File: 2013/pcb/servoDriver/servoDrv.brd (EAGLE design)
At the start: 20.3 x 16.5 mm, 9 parts, among them X1 22-23-2041

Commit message: servodriveriin tehty muutoksia. Sense-vastukset paremmin gnd-planeen.
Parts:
- moved RSENS_B 10.0 mm to (8.39, 11.5), turned to 0 degrees
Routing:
- net N$4: track 8.46 -> 0.00 mm
- net VCC: track 0.00 -> 7.28 mm
- removed copper zone on layer 16, net VCC
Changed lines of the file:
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@@
 <plain>
 <wire x1="0" y1="0" x2="20.32" y2="0" width="0" layer="20"/>
-<wire x1="20.32" y1="0" x2="20.32" y2="16.5" width="0" layer="20"/>
 <wire x1="20.32" y1="16.5" x2="0" y2="16.5" width="0" layer="20"/>
 <wire x1="0" y1="16.5" x2="0" y2="0" width="0" layer="20"/>
@@
 </element>
 <element name="RSENS_A" library="resistor" package="R1206" value="" x="8.45" y="4.06" rot="MR180"/>
-<element name="RSENS_B" library="resistor" package="R1206" value="" x="12.94" y="2.61" rot="MR90"/>
+<element name="RSENS_B" library="resistor" package="R1206" value="" x="8.39" y="11.54" rot="MR0"/>
 <element name="RIN_A" library="resistor" package="R0805" value="" x="7.96" y="3.63"/>
 <element name="RIN_B" library="resistor" package="R0805" value="" x="8.01" y="11.23"/>
@@
 <contactref element="C2" pad="1"/>
 <contactref element="X1" pad="2"/>
-<polygon width="0.3048" layer="16">
-<vertex x="-0.2" y="10"/>
-<vertex x="-0.2" y="16.8"/>
-<vertex x="20.6" y="16.8"/>
-<vertex x="20.6" y="10.8"/>
-<vertex x="8.2" y="10.8"/>
-<vertex x="8.2" y="8.2"/>
-<vertex x="-0.2" y="8.2"/>
-</polygon>
-<wire x1="7.27" y1="8.51" x2="9.3884" y2="8.455" width="0" layer="19" extent="16-16"/>
+<wire x1="2.34015625" y1="8.87005" x2="4.63995" y2="8.87005" width="1.016" layer="16"/>
+<wire x1="4.63995" y1="8.87005" x2="5.07" y2="8.44" width="1.016" layer="16"/>
+<wire x1="5.07" y1="8.44" x2="7.2" y2="8.44" width="1.016" layer="16"/>
+<wire x1="7.2" y1="8.44" x2="7.27" y2="8.51" width="1.016" layer="16"/>
+<wire x1="7.27" y1="8.51" x2="9.3334" y2="8.51" width="1.016" layer="16"/>
+<wire x1="9.3334" y1="8.51" x2="9.3884" y2="8.455" width="1.016" layer="16"/>
 </signal>
 <signal name="GND">
@@
 <contactref element="C2" pad="2"/>
 <contactref element="X1" pad="3"/>
-<polygon width="0.3048" layer="16">
-<vertex x="-0.2" y="16.6"/>
-<vertex x="20.6" y="16.6"/>
-<vertex x="20.6" y="11.4"/>
-<vertex x="13.4" y="11.4"/>
-<vertex x="13.4" y="4.2"/>
-<vertex x="20.6" y="4.2"/>
-<vertex x="20.6" y="-0.4"/>
-<vertex x="-0.4" y="-0.4"/>
-<vertex x="-0.4" y="16.6"/>
-</polygon>
 <polygon width="0.3048" layer="1">
 <vertex x="-0.2" y="16.6"/>
@@
 <vertex x="-0.2" y="-0.2"/>
 </polygon>
+<polygon width="0.3048" layer="16">
+<vertex x="-0.2" y="16.4"/>
+<vertex x="20.4" y="16.4"/>
+<vertex x="20.4" y="16.2"/>
+<vertex x="20.4" y="0"/>
+<vertex x="0" y="0"/>
+<vertex x="0" y="0.2"/>
+<vertex x="-0.2" y="0.2"/>
+</polygon>
 </signal>
 <signal name="N$1">
@@
 <contactref element="U1" pad="4"/>
 <contactref element="RSENS_B" pad="2"/>
-<wire x1="9.3884" y1="9.725" x2="11.6" y2="9.725" width="0.3048" layer="16"/>
-<wire x1="11.6" y1="9.725" x2="11.6" y2="5.372" width="0.3048" layer="16"/>
-<wire x1="11.6" y1="5.372" x2="12.94" y2="4.032" width="0.3048" layer="16"/>
+<wire x1="6.968" y1="11.54" x2="9.3884" y2="9.725" width="0" layer="19" extent="16-16"/>
 </signal>
 <signal name="N$6">

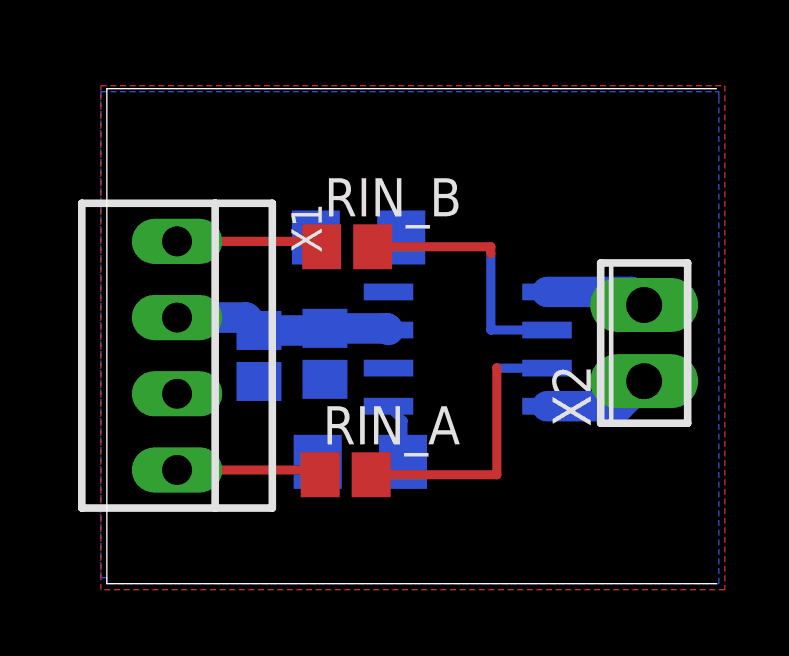
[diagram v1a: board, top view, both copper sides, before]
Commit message: servodriverin skemaa muutettu, lisätty tvs:t inputteihin ja poistettu sense-vastukset. Myös puuttuvat viat lisätty.
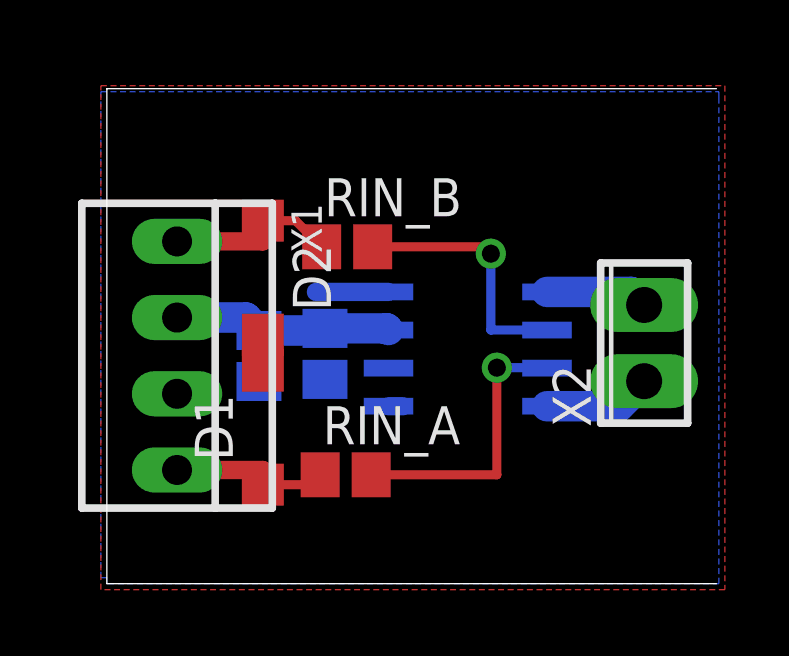
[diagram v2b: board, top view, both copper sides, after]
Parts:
- removed RSENS_A, RSENS_B: (no value), resistor:R1206
- added D1, D2: (no value), diode:SOD123
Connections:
- removed net N$3: RSENS_A.2, U1.1
- removed net N$4: RSENS_B.2, U1.4
- net GND: now also D1.A, D2.A, U1.1, U1.4; no longer RSENS_A.1, RSENS_B.1
- net N$5: now also D1.C
- net N$8: now also D2.C
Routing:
- net GND: track 0.00 -> 2.90 mm
- net N$3: track 2.06 -> 0.00 mm
- net N$8: track 4.89 -> 5.87 mm
- net N$7: track 8.59 -> 8.45 mm, vias 0 -> 1
- net N$6: vias 0 -> 1
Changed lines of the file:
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@@
 <attribute name="OC_FARNELL" value="unknown" x="31.88" y="24.53" size="1.778" layer="27" rot="R90" display="off"/>
 </element>
-<element name="RSENS_A" library="resistor" package="R1206" value="" x="8.45" y="4.06" rot="MR180"/>
-<element name="RSENS_B" library="resistor" package="R1206" value="" x="8.39" y="11.54" rot="MR0"/>
 <element name="RIN_A" library="resistor" package="R0805" value="" x="7.96" y="3.63"/>
 <element name="RIN_B" library="resistor" package="R0805" value="" x="8.01" y="11.23"/>
 <element name="C1" library="resistor" package="C0805" value="" x="5.07" y="7.59" rot="MR270"/>
 <element name="C2" library="resistor" package="C0805" value="" x="7.27" y="7.66" rot="MR270"/>
+<element name="D1" library="diode" package="SOD123" value="" x="5.2" y="5.2" rot="R90"/>
+<element name="D2" library="diode" package="SOD123" value="" x="5.2" y="10.2" rot="R270"/>
 </elements>
 <signals>
@@
 </signal>
 <signal name="GND">
-<contactref element="U1" pad="2"/>
-<contactref element="RSENS_B" pad="1"/>
-<contactref element="RSENS_A" pad="1"/>
 <contactref element="C1" pad="2"/>
 <contactref element="C2" pad="2"/>
@@
 <vertex x="-0.2" y="0.2"/>
 </polygon>
+<contactref element="U1" pad="1"/>
+<wire x1="9.3884" y1="5.915" x2="9.872" y2="5.915" width="0.6096" layer="16"/>
+<contactref element="U1" pad="4"/>
+<wire x1="9.3884" y1="9.725" x2="6.968" y2="9.725" width="0.6096" layer="16"/>
+<contactref element="U1" pad="2"/>
+<contactref element="D1" pad="A"/>
+<contactref element="D2" pad="A"/>
 </signal>
 <signal name="N$1">
@@
 <wire x1="17.475" y1="9.725" x2="17.91" y2="9.29" width="1.016" layer="16"/>
 </signal>
-<signal name="N$3">
-<contactref element="RSENS_A" pad="2"/>
-<contactref element="U1" pad="1"/>
-<wire x1="9.3884" y1="5.915" x2="9.872" y2="5.4314" width="0.3048" layer="16"/>
-<wire x1="9.872" y1="5.4314" x2="9.872" y2="4.06" width="0.3048" layer="16"/>
-</signal>
-<signal name="N$4">
-<contactref element="U1" pad="4"/>
-<contactref element="RSENS_B" pad="2"/>
-<wire x1="6.968" y1="11.54" x2="9.3884" y2="9.725" width="0" layer="19" extent="16-16"/>
-</signal>
 <signal name="N$6">
 <contactref element="RIN_A" pad="2"/>
 <contactref element="U1" pad="7"/>
-<wire x1="8.81" y1="3.63" x2="13" y2="3.63" width="0.3048" layer="1"/>
-<wire x1="13" y1="3.63" x2="13" y2="7.2" width="0.3048" layer="1"/>
-<wire x1="14.6716" y1="7.185" x2="13" y2="7.185" width="0.3048" layer="16"/>
-<wire x1="13" y1="7.185" x2="13" y2="7.2" width="0.3048" layer="16"/>
-<wire x1="13" y1="7.2" x2="13" y2="7.2" width="0" layer="19" extent="1-16"/>
+<wire x1="14.6716" y1="7.185" x2="14.6716" y2="7.2" width="0.3048" layer="16"/>
+<wire x1="14.6716" y1="7.2" x2="13" y2="7.2" width="0.3048" layer="16"/>
+<via x="13" y="7.2" extent="1-16" drill="0.6" shape="square"/>
+<wire x1="13" y1="7.2" x2="13" y2="3.63" width="0.3048" layer="1"/>
+<wire x1="13" y1="3.63" x2="8.81" y2="3.63" width="0.3048" layer="1"/>
 </signal>
 <signal name="N$7">
 <contactref element="RIN_B" pad="2"/>
 <contactref element="U1" pad="6"/>
-<wire x1="8.86" y1="11.23" x2="12.8" y2="11.23" width="0.3048" layer="1"/>
-<wire x1="12.8" y1="11.23" x2="12.8" y2="11" width="0.3048" layer="1"/>
-<wire x1="14.6716" y1="8.455" x2="12.8" y2="8.455" width="0.3048" layer="16"/>
-<wire x1="12.8" y1="8.455" x2="12.8" y2="11" width="0.3048" layer="16"/>
-<wire x1="12.8" y1="11" x2="12.8" y2="11" width="0" layer="19" extent="1-16"/>
+<wire x1="8.86" y1="11.23" x2="12.57" y2="11.23" width="0.3048" layer="1"/>
+<wire x1="12.57" y1="11.23" x2="12.8" y2="11" width="0.3048" layer="1"/>
+<via x="12.8" y="11" extent="1-16" drill="0.6" shape="square"/>
+<wire x1="12.8" y1="11" x2="12.8" y2="8.455" width="0.3048" layer="16"/>
+<wire x1="12.8" y1="8.455" x2="14.6716" y2="8.455" width="0.3048" layer="16"/>
 </signal>
 <signal name="N$8">
 <contactref element="X1" pad="1"/>
 <contactref element="RIN_B" pad="1"/>
-<wire x1="6.97995" y1="11.41005" x2="7.16" y2="11.23" width="1.016" layer="1"/>
-<wire x1="2.34015625" y1="11.41005" x2="6.97995" y2="11.41005" width="0.3048" layer="1"/>
+<contactref element="D2" pad="C"/>
+<wire x1="2.34015625" y1="11.41005" x2="5.2" y2="11.41005" width="0.6096" layer="1"/>
+<wire x1="5.2" y1="11.41005" x2="5.2" y2="12.1" width="0.6096" layer="1"/>
+<wire x1="7.16" y1="11.23" x2="6.29" y2="12.1" width="0.3048" layer="1"/>
+<wire x1="6.29" y1="12.1" x2="5.2" y2="12.1" width="0.3048" layer="1"/>
 </signal>
 <signal name="N$5">
 <contactref element="X1" pad="4"/>
 <contactref element="RIN_A" pad="1"/>
-<wire x1="2.34015625" y1="3.79005" x2="7.11" y2="3.79005" width="0.3048" layer="1"/>
-<wire x1="7.11" y1="3.79005" x2="7.11" y2="3.63" width="0.3048" layer="1"/>
+<contactref element="D1" pad="C"/>
+<wire x1="2.34015625" y1="3.79005" x2="5.2" y2="3.79005" width="0.6096" layer="1"/>
+<wire x1="5.2" y1="3.79005" x2="5.2" y2="3.3" width="0.6096" layer="1"/>
+<wire x1="7.11" y1="3.63" x2="6.78" y2="3.3" width="0.3048" layer="1"/>
+<wire x1="6.78" y1="3.3" x2="5.2" y2="3.3" width="0.3048" layer="1"/>
 </signal>
 </signals>

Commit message: Lisää muutoksia servodriveriin, board outline lisätty.
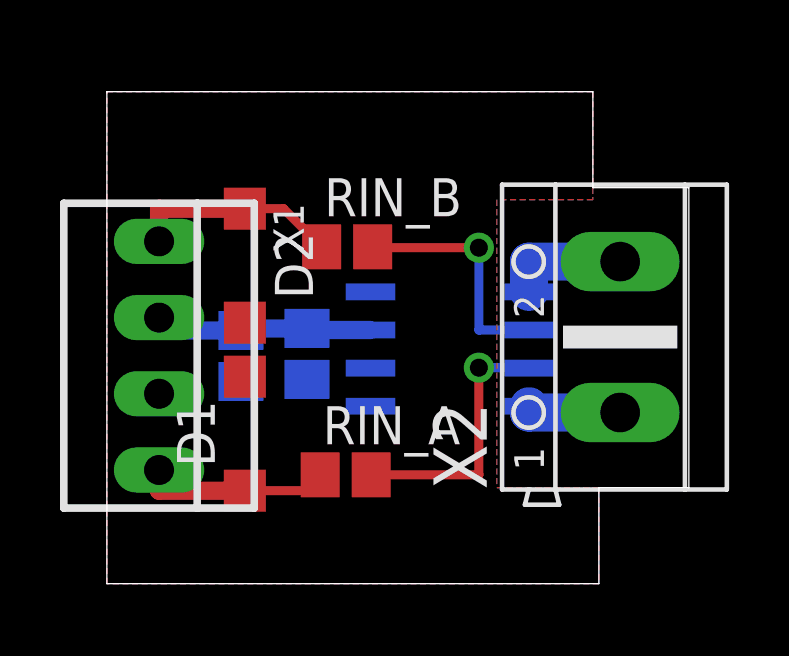
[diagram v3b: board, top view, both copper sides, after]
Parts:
- X2: device con-phoenix-254:2POL254 -> con-ptr500:AK500/2
- moved X2 0.82 mm to (17.1, 8.22)
- moved D2 0.72 mm to (4.60, 10.6)
- moved D1 0.63 mm to (4.60, 5.00)
- moved C1 0.60 mm to (4.47, 7.59)
- moved X1 0.60 mm to (1.74, 7.60)
- moved C2 0.60 mm to (6.67, 7.66)
- moved U1 0.60 mm to (11.4, 7.82)
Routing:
- net GND: track 2.90 -> 0.00 mm
- net N$8: track 5.87 -> 7.04 mm
- net N$5: track 5.40 -> 6.28 mm
- net N$2: track 3.42 -> 4.05 mm
- net N$6: track 9.45 -> 10.0 mm
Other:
- board size 20.3 x 16.5 mm -> 19.4 x 16.4 mm

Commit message: viimeisin versio servodriverista
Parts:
- C1: value (none) -> 100n
- C2: value (none) -> 1u
- D1, D2: value (none) -> PTVS6V0S1UR
- RIN_A, RIN_B: value (none) -> 100
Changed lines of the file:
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@@
 <attribute name="OC_FARNELL" value="unknown" x="31.08" y="24.73" size="1.778" layer="27" rot="R90" display="off"/>
 </element>
-<element name="RIN_A" library="resistor" package="R0805" value="" x="7.96" y="3.63"/>
-<element name="RIN_B" library="resistor" package="R0805" value="" x="8.01" y="11.23"/>
-<element name="C1" library="resistor" package="C0805" value="" x="4.47" y="7.59" rot="MR270"/>
-<element name="C2" library="resistor" package="C0805" value="" x="6.67" y="7.66" rot="MR270"/>
-<element name="D1" library="diode" package="SOD123" value="" x="4.6" y="5" rot="R90"/>
-<element name="D2" library="diode" package="SOD123" value="" x="4.6" y="10.6" rot="R270"/>
+<element name="RIN_A" library="resistor" package="R0805" value="100" x="7.96" y="3.63"/>
+<element name="RIN_B" library="resistor" package="R0805" value="100" x="8.01" y="11.23"/>
+<element name="C1" library="resistor" package="C0805" value="100n" x="4.47" y="7.59" rot="MR270"/>
+<element name="C2" library="resistor" package="C0805" value="1u" x="6.67" y="7.66" rot="MR270"/>
+<element name="D1" library="diode" package="SOD123" value="PTVS6V0S1UR" x="4.6" y="5" rot="R90"/>
+<element name="D2" library="diode" package="SOD123" value="PTVS6V0S1UR" x="4.6" y="10.6" rot="R270"/>
 </elements>
 <signals>

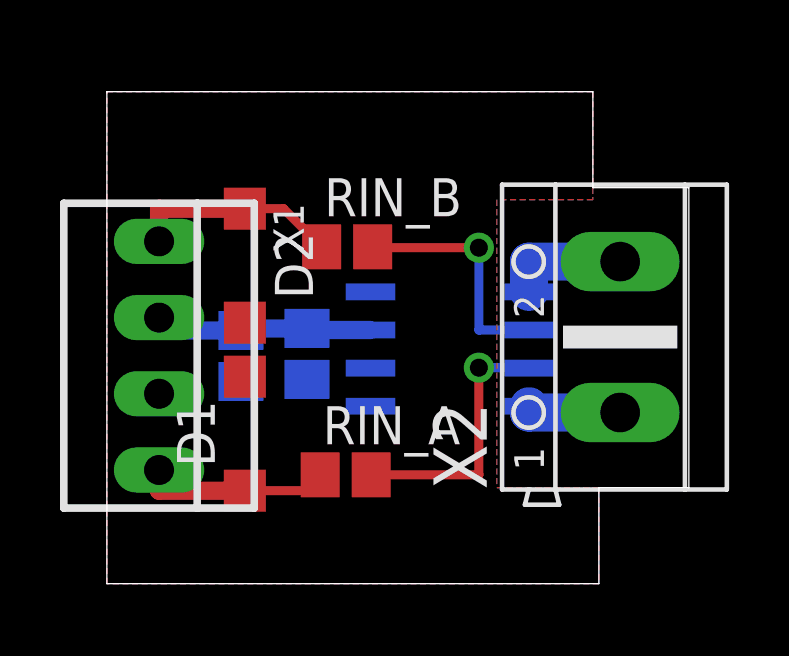
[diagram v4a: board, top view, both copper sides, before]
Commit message: Muutettu servoDriver pcb yksipuoleiseksi
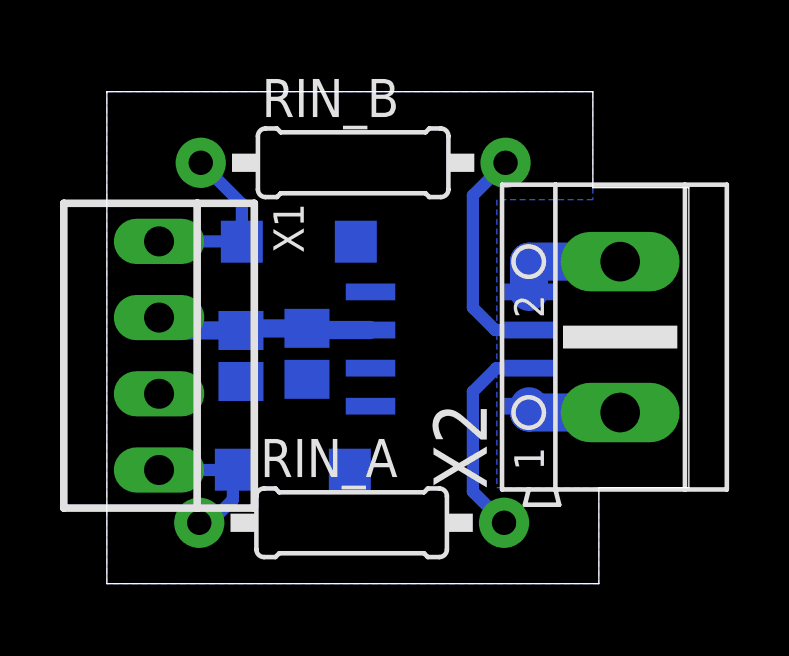
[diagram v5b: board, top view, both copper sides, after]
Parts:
- RIN_A, RIN_B: device resistor:R0805 -> resistor2:0207/10
- moved RIN_B 2.81 mm to (8.21, 14.0)
- moved D1 2.00 mm to (6.20, 3.80), flipped to the bottom, turned to 180 degrees
- moved D2 1.97 mm to (6.40, 11.4), flipped to the bottom, turned to 180 degrees
- moved RIN_A 1.61 mm to (8.16, 2.03)
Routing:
- net N$6: track 10.0 -> 7.00 mm, vias 1 -> 0
- net N$5: track 6.28 -> 5.04 mm
- net N$8: track 7.04 -> 5.97 mm
- net N$7: track 7.97 -> 7.46 mm, vias 1 -> 0
- removed copper zone on layer 1, net GND
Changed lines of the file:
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@@
 <?xml version="1.0" encoding="utf-8"?>
 <!DOCTYPE eagle SYSTEM "eagle.dtd">
-<eagle version="6.5.0">
+<eagle version="6.4">
 <drawing>
 <settings>
@@
 <layer number="23" name="tOrigins" color="15" fill="1" visible="yes" active="yes"/>
 <layer number="24" name="bOrigins" color="15" fill="1" visible="yes" active="yes"/>
-<layer number="25" name="tNames" color="7" fill="1" visible="yes" active="yes"/>
-<layer number="26" name="bNames" color="7" fill="1" visible="yes" active="yes"/>
-<layer number="27" name="tValues" color="7" fill="1" visible="yes" active="yes"/>
-<layer number="28" name="bValues" color="7" fill="1" visible="yes" active="yes"/>
+<layer number="25" name="tNames" color="7" fill="1" visible="no" active="yes"/>
+<layer number="26" name="bNames" color="7" fill="1" visible="no" active="yes"/>
+<layer number="27" name="tValues" color="7" fill="1" visible="no" active="yes"/>
+<layer number="28" name="bValues" color="7" fill="1" visible="no" active="yes"/>
 <layer number="29" name="tStop" color="7" fill="3" visible="no" active="yes"/>
 <layer number="30" name="bStop" color="7" fill="6" visible="no" active="yes"/>
@@
 </class>
 </classes>
-<designrules name="default">
+<designrules name="default *">
 <description language="de">&lt;b&gt;EAGLE Design Rules&lt;/b&gt;
 &lt;p&gt;
@@
 <attribute name="OC_FARNELL" value="unknown" x="31.08" y="24.73" size="1.778" layer="27" rot="R90" display="off"/>
 </element>
-<element name="RIN_A" library="resistor" package="R0805" value="100" x="7.96" y="3.63"/>
-<element name="RIN_B" library="resistor" package="R0805" value="100" x="8.01" y="11.23"/>
+<element name="RIN_A" library="resistor2" package="0207/10" value="100" x="8.16" y="2.03"/>
+<element name="RIN_B" library="resistor2" package="0207/10" value="100" x="8.21" y="14.03"/>
 <element name="C1" library="resistor" package="C0805" value="100n" x="4.47" y="7.59" rot="MR270"/>
 <element name="C2" library="resistor" package="C0805" value="1u" x="6.67" y="7.66" rot="MR270"/>
-<element name="D1" library="diode" package="SOD123" value="PTVS6V0S1UR" x="4.6" y="5" rot="R90"/>
-<element name="D2" library="diode" package="SOD123" value="PTVS6V0S1UR" x="4.6" y="10.6" rot="R270"/>
+<element name="D1" library="diode" package="SOD123" value="PTVS6V0S1UR" x="6.2" y="3.8" rot="MR180"/>
+<element name="D2" library="diode" package="SOD123" value="PTVS6V0S1UR" x="6.4" y="11.4" rot="MR180"/>
 </elements>
 <signals>
@@
 <vertex x="0" y="0"/>
 </polygon>
-<polygon width="0.254" layer="1">
-<vertex x="0" y="16.4"/>
-<vertex x="16.2" y="16.4"/>
-<vertex x="16.2" y="12.8"/>
-<vertex x="13" y="12.8"/>
-<vertex x="13" y="3.2"/>
-<vertex x="16.4" y="3.2"/>
-<vertex x="16.4" y="0"/>
-<vertex x="0" y="0"/>
-</polygon>
 </signal>
 <signal name="N$1">
@@
 <contactref element="RIN_A" pad="2"/>
 <contactref element="U1" pad="7"/>
-<wire x1="14.0716" y1="7.185" x2="14.6716" y2="7.2" width="0.3048" layer="16"/>
-<wire x1="14.6716" y1="7.2" x2="12.4" y2="7.2" width="0.3048" layer="16"/>
-<via x="12.4" y="7.2" extent="1-16" drill="0.6" shape="square"/>
-<wire x1="12.4" y1="7.2" x2="12.4" y2="3.63" width="0.3048" layer="1"/>
-<wire x1="12.4" y1="3.63" x2="8.81" y2="3.63" width="0.3048" layer="1"/>
+<wire x1="14.0716" y1="7.185" x2="12.985" y2="7.185" width="0.4064" layer="16"/>
+<wire x1="12.985" y1="7.185" x2="12.2" y2="6.4" width="0.4064" layer="16"/>
+<wire x1="12.2" y1="6.4" x2="12.2" y2="3.07" width="0.4064" layer="16"/>
+<wire x1="12.2" y1="3.07" x2="13.24" y2="2.03" width="0.4064" layer="16"/>
 </signal>
 <signal name="N$7">
 <contactref element="RIN_B" pad="2"/>
 <contactref element="U1" pad="6"/>
-<wire x1="8.86" y1="11.23" x2="8.89" y2="11.2" width="0.3048" layer="1"/>
-<wire x1="8.89" y1="11.2" x2="12.4" y2="11.2" width="0.3048" layer="1"/>
-<via x="12.4" y="11.2" extent="1-16" drill="0.6" shape="square"/>
-<wire x1="12.4" y1="11.2" x2="12.4" y2="8.455" width="0.3048" layer="16"/>
-<wire x1="12.4" y1="8.455" x2="14.0716" y2="8.455" width="0.3048" layer="16"/>
+<wire x1="13.29" y1="14.03" x2="12.2" y2="12.94" width="0.4064" layer="16"/>
+<wire x1="12.2" y1="12.94" x2="12.2" y2="9.2" width="0.4064" layer="16"/>
+<wire x1="12.2" y1="9.2" x2="12.945" y2="8.455" width="0.4064" layer="16"/>
+<wire x1="12.945" y1="8.455" x2="14.0716" y2="8.455" width="0.4064" layer="16"/>
 </signal>
 <signal name="N$8">
@@
 <contactref element="RIN_B" pad="1"/>
 <contactref element="D2" pad="C"/>
-<wire x1="1.74015625" y1="11.41005" x2="1.74015625" y2="12.5" width="0.6096" layer="1"/>
-<wire x1="1.74015625" y1="12.5" x2="4.6" y2="12.5" width="0.6096" layer="1"/>
-<wire x1="7.16" y1="11.23" x2="5.89" y2="12.5" width="0.3048" layer="1"/>
-<wire x1="5.89" y1="12.5" x2="4.6" y2="12.5" width="0.3048" layer="1"/>
+<wire x1="1.74015625" y1="11.41005" x2="4.5" y2="11.41005" width="0.4064" layer="16"/>
+<wire x1="4.5" y1="11.41005" x2="4.5" y2="11.4" width="0.4064" layer="16"/>
+<wire x1="4.5" y1="11.4" x2="4.5" y2="12.66" width="0.4064" layer="16"/>
+<wire x1="4.5" y1="12.66" x2="3.13" y2="14.03" width="0.4064" layer="16"/>
 </signal>
 <signal name="N$5">
@@
 <contactref element="RIN_A" pad="1"/>
 <contactref element="D1" pad="C"/>
-<wire x1="1.74015625" y1="3.79005" x2="1.74015625" y2="3.1" width="0.6096" layer="1"/>
-<wire x1="1.74015625" y1="3.1" x2="4.6" y2="3.1" width="0.6096" layer="1"/>
-<wire x1="4.6" y1="3.1" x2="6.58" y2="3.1" width="0.3048" layer="1"/>
-<wire x1="6.58" y1="3.1" x2="7.11" y2="3.63" width="0.3048" layer="1"/>
+<wire x1="1.74015625" y1="3.79005" x2="4.29005" y2="3.79005" width="0.4064" layer="16"/>
+<wire x1="4.29005" y1="3.79005" x2="4.3" y2="3.8" width="0.4064" layer="16"/>
+<wire x1="3.08" y1="2.03" x2="3.43" y2="2.03" width="0.4064" layer="16"/>
+<wire x1="3.43" y1="2.03" x2="4.2" y2="2.8" width="0.4064" layer="16"/>
+<wire x1="4.2" y1="2.8" x2="4.2" y2="3.7" width="0.4064" layer="16"/>
+<wire x1="4.2" y1="3.7" x2="4.3" y2="3.8" width="0.4064" layer="16"/>
 </signal>
 </signals>
